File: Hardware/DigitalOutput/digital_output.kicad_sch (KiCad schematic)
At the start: 40 parts, among them Q10 SI2347DS, Q11 SI2347DS, Q12 SI2347DS, Q13 SI2347DS, Q14 SI2347DS, Q15 SI2347DS, Q16 SI2347DS, Q9 SI2347DS, U10 CNY17-3, U11 CNY17-3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

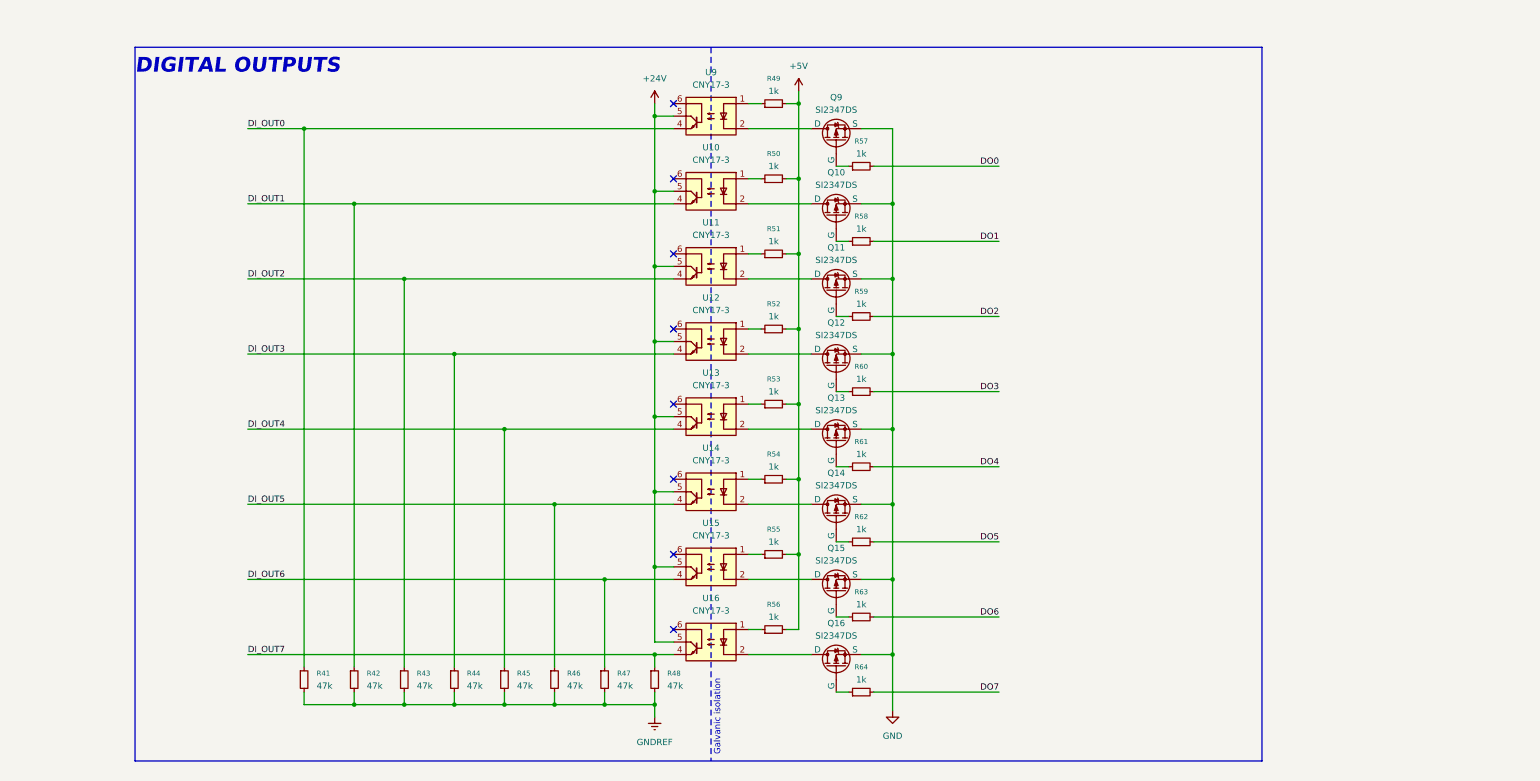
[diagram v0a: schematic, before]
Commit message: digital output & digital input update
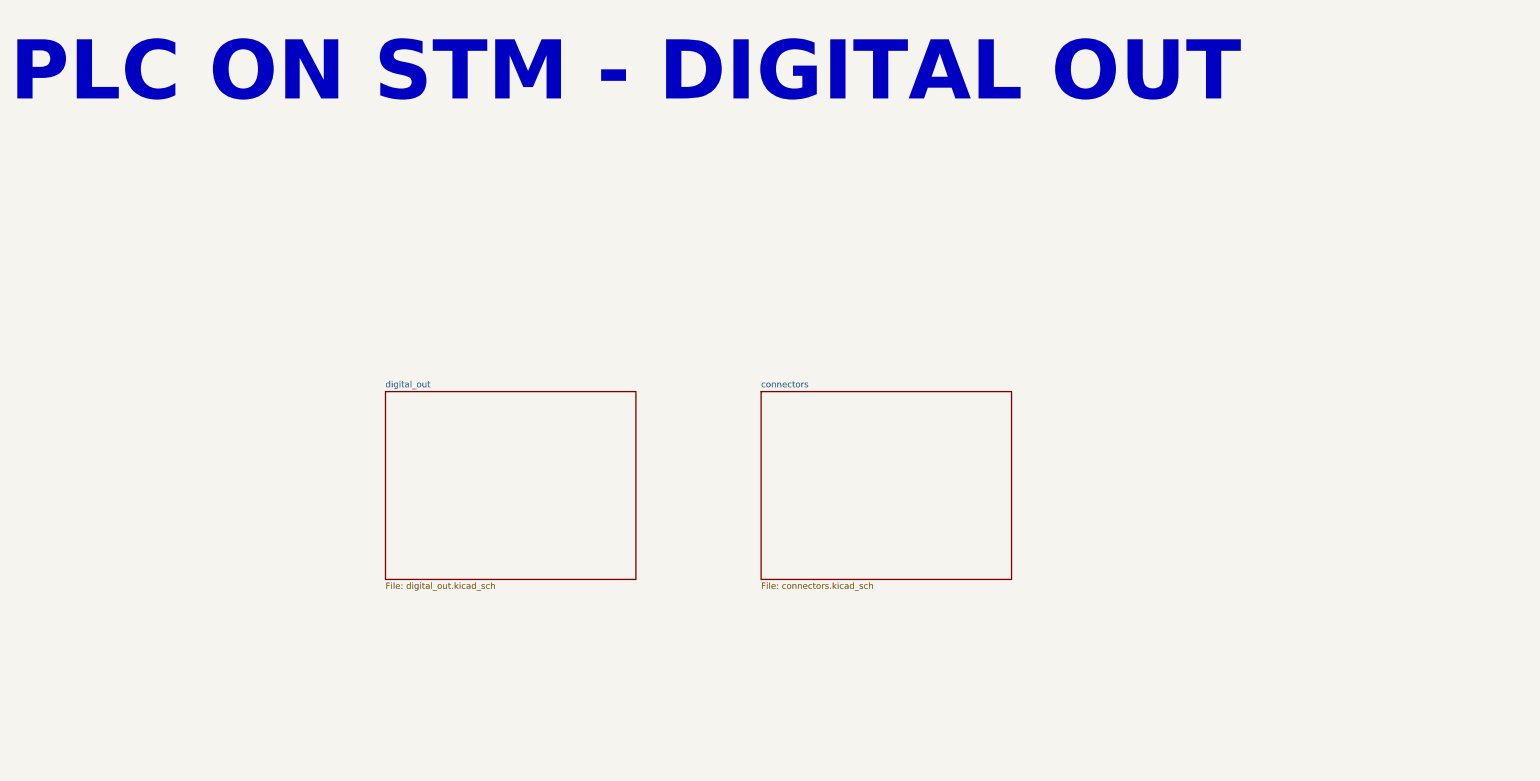
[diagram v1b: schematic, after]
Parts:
- removed Q10, Q11, Q12, Q13, Q14, Q15, Q16, Q9: SI2347DS, Package_TO_SOT_SMD:SOT-23-3, symbol Simulation_SPICE:PMOS
- removed R41, R42, R43, R44, R45, R46, R47, R48: 47k, Resistor_SMD:R_0603_1608Metric_Pad0.98x0.95mm_HandSolder, symbol Device:R_Small
- removed R49, R50, R51, R52, R53, R54, R55, R56, R57, R58, R59, R60, R61, R62, R63, R64: 1k, Resistor_SMD:R_0603_1608Metric_Pad0.98x0.95mm_HandSolder, symbol Device:R_Small
- removed U10, U11, U12, U13, U14, U15, U16, U9: CNY17-3, PLC_STM:SOP254P1016X400-6N, symbol Isolator:CNY17-3
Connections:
- no-connect marks 8 -> 0
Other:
- added sheet connectors (connectors.kicad_sch)
- added sheet digital_out (digital_out.kicad_sch)
- note added: "PLC ON STM - DIGITAL OUT"
- note removed: "DIGITAL OUTPUTS"
- note removed: "Galvanic isolation"
- title: PLC on STM - Digital IO Shield -> PLC on STM - Digital Output Shield
